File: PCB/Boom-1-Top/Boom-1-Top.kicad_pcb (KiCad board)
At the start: 4 copper layers, 345 x 165 mm, 768 parts, among them J1 DEBUG, J10 PIC_DEBUG, J11 PIC_DEBUG, J12 PIC_DEBUG, J13 PIC_DEBUG, J14 PIC_DEBUG, J15 USB_B_Micro, J16 SD_Card, J17 BT_DEBUG, J18 12V Supply, J19 3V3 Bypass, J2 MIDI IN, J20 5V Bypass, J3 MIDI OUT, J37 Osc1Conn, J38 Osc2Conn, J39 SubNoiseConn, J4 PIC_DEBUG, J40 FiltConn2, J41 EnvGenConn2, J42 EnvGenConn1, J43 FXConn1, J44 FiltConn1, J45 FXConn2, J46 EnvGenConn3, J5 PIC_DEBUG, J6 PIC_DEBUG, J7 PIC_DEBUG, J8 PIC_DEBUG, J9 PIC_DEBUG, Q1 AO3401A, Q2 AO3401A, SW1 Osc1SawEncoder, SW10 SubToOsc2FiltEncoder, SW11 Osc1ToOsc2FiltEncoder, SW12 Osc1FiltFreqEncoder, SW13 Osc2FiltFreqEncoder, SW14 SubFiltFreqEncoder, SW15 OscFiltEnvAttackEncoder, SW16 SubFiltEnvAttackEncoder, SW17 Osc1FiltResEncoder, SW18 Osc2FiltResEncoder, SW19 SubFiltResEncoder, SW2 Osc1SqrEncoder, SW20 OscFiltEnvDecayEncoder, SW21 SubFiltEnvDecayEncoder, SW22 OscFiltEnvSustainEncoder, SW23 SubFiltEnvSustainEncoder, SW24 Osc1DriveEncoder, SW25 Osc2DistortionEncoder, SW26 OscFiltEnvReleaseEncoder, SW27 SubFiltEnvReleaseEncoder, SW28 FXWetDryEncoder, SW29 SubAmpEnvAttackEncoder, SW3 Rotary_Encoder, SW30 OscAmpEnvAttackEncoder, SW31 FXControl1Encoder, SW32 SubAmpEnvDecayEncoder, SW33 OscAmpEnvDecayEncoder, SW34 FXControl2Encoder, SW35 SubAmpEnvSustainEncoder, SW36 OscAmpEnvSustainEncoder, SW37 FXControl3Encoder, SW38 FXFeedbackEncoder, SW39 SubAmpEnvReleaseEncoder, SW4 Rotary_Encoder_Switch, SW40 OscAmpEnvReleaseEncoder, SW41 Reset, SW43 Reset, SW5 Rotary_Encoder, SW53 Osc1TuneEncoder, SW6 SubToSubFiltEncoder, SW7 SubNoiseEncoder, U1 STM32F407VGTx, U10 DAC7678xPW, U11 PIC18F26Q43, U12 PIC18F26Q43, U13 PIC18F26Q43, U14 PIC18F26Q43, U15 PIC18F26Q43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

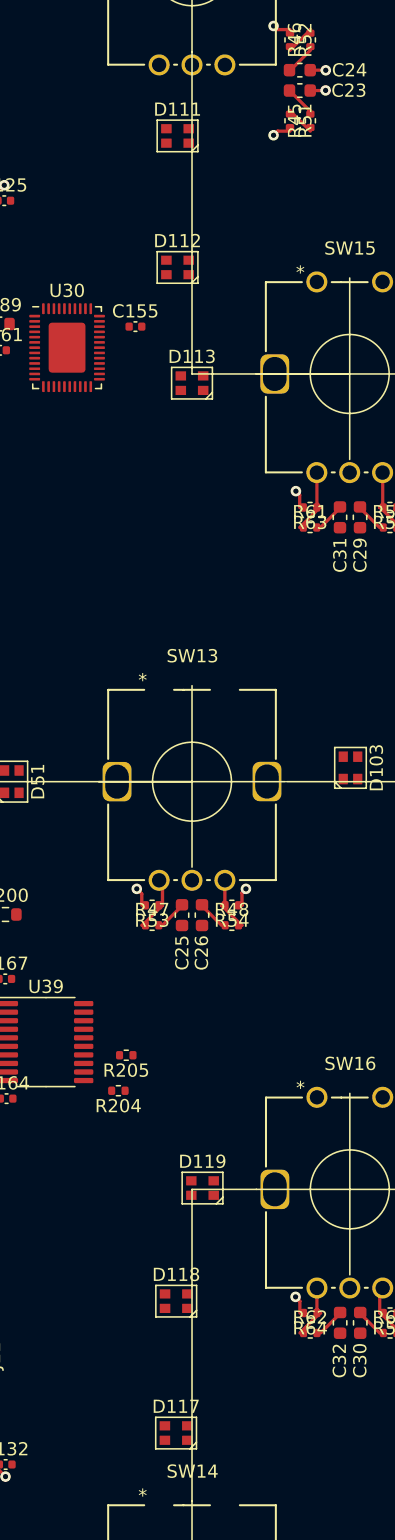
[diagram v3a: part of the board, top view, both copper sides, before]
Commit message: WIP, but crashed on open on discrete GPU machine
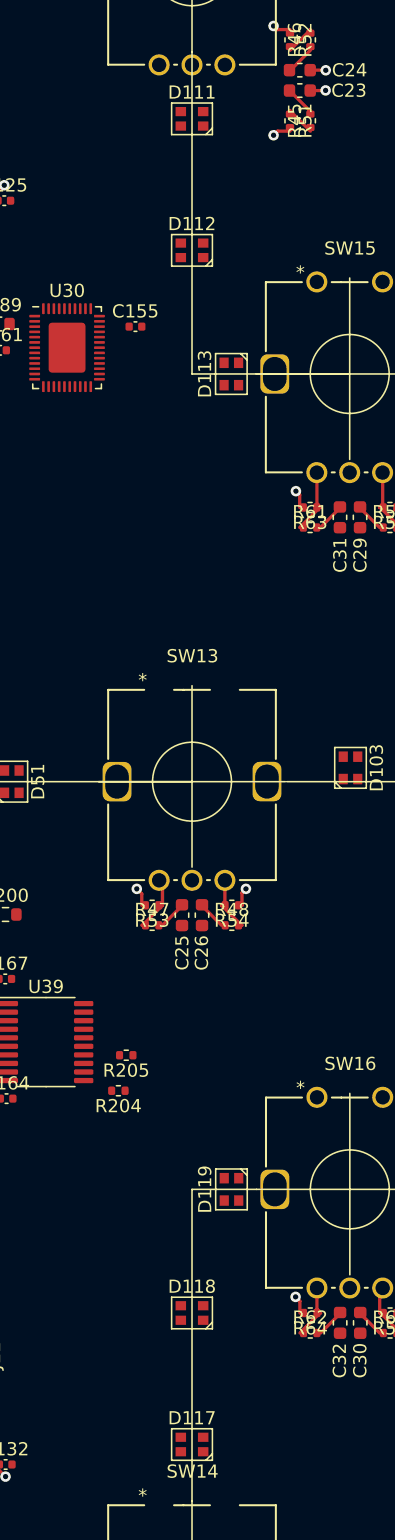
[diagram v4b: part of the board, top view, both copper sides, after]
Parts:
- moved D113 3.07 mm to (239.5, 156.2), turned to 90 degrees
- moved D119 2.20 mm to (239.5, 218.2), turned to 90 degrees
- moved D111 1.70 mm to (236.5, 136.8)
- moved D112 1.70 mm to (236.5, 146.8)
- moved D118 1.50 mm to (236.5, 227.6)
- moved D117 1.49 mm to (236.5, 237.6)
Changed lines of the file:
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@@
   )
   (module fm-b2020rgba-hg:FM-B2020RGBA-HG (layer F.Cu)
-    (at 237.3 218.1)
+    (at 239.5 218.2 90)
     (attr smd)
-    (fp_text reference D119 (at 0 -2) (layer F.SilkS)
+    (fp_text reference D119 (at 0 -2 90) (layer F.SilkS)
       (effects (font (size 1 1) (thickness 0.15)))
     )
-    (fp_text value SubFiltEnvLED3 (at 0 2.05) (layer F.Fab)
+    (fp_text value SubFiltEnvLED3 (at 0 2.05 90) (layer F.Fab)
       (effects (font (size 1 1) (thickness 0.15)))
     )
@@
     (fp_line (start 1.25 0.9) (end -1.25 0.9) (layer F.CrtYd) (width 0.12))
     (fp_line (start 1.25 0) (end 1.25 0.9) (layer F.CrtYd) (width 0.12))
-    (pad 4 smd rect (at 0.85 -0.55) (size 0.8 0.7) (layers F.Cu F.Paste F.Mask)
+    (pad 4 smd rect (at 0.85 -0.55 90) (size 0.8 0.7) (layers F.Cu F.Paste F.Mask)
       (net 859 L6G6))
-    (pad 3 smd rect (at -0.85 -0.55) (size 0.8 0.7) (layers F.Cu F.Paste F.Mask)
+    (pad 3 smd rect (at -0.85 -0.55 90) (size 0.8 0.7) (layers F.Cu F.Paste F.Mask)
       (net 1346 "Net-(D119-Pad3)"))
-    (pad 2 smd rect (at -0.85 0.55) (size 0.8 0.7) (layers F.Cu F.Paste F.Mask)
+    (pad 2 smd rect (at -0.85 0.55 90) (size 0.8 0.7) (layers F.Cu F.Paste F.Mask)
       (net 860 L6B6))
-    (pad 1 smd rect (at 0.85 0.55) (size 0.8 0.7) (layers F.Cu F.Paste F.Mask)
+    (pad 1 smd rect (at 0.85 0.55 90) (size 0.8 0.7) (layers F.Cu F.Paste F.Mask)
       (net 858 L6R6))
   )
   (module fm-b2020rgba-hg:FM-B2020RGBA-HG (layer F.Cu)
-    (at 235.3 226.7)
+    (at 236.5 227.6)
     (attr smd)
     (fp_text reference D118 (at 0 -2) (layer F.SilkS)
@@
   )
   (module fm-b2020rgba-hg:FM-B2020RGBA-HG (layer F.Cu)
-    (at 235.29 236.73)
+    (at 236.5 237.6)
     (attr smd)
     (fp_text reference D117 (at 0 -2) (layer F.SilkS)
@@
   )
   (module fm-b2020rgba-hg:FM-B2020RGBA-HG (layer F.Cu)
-    (at 236.5 156.9)
+    (at 239.49 156.2 90)
     (attr smd)
-    (fp_text reference D113 (at 0 -2) (layer F.SilkS)
+    (fp_text reference D113 (at 0 -2 90) (layer F.SilkS)
       (effects (font (size 1 1) (thickness 0.15)))
     )
-    (fp_text value OscFiltEnvLED3 (at 0 2.05) (layer F.Fab)
+    (fp_text value OscFiltEnvLED3 (at 0 2.05 90) (layer F.Fab)
       (effects (font (size 1 1) (thickness 0.15)))
     )
@@
     (fp_line (start 1.25 0.9) (end -1.25 0.9) (layer F.CrtYd) (width 0.12))
     (fp_line (start 1.25 0) (end 1.25 0.9) (layer F.CrtYd) (width 0.12))
-    (pad 4 smd rect (at 0.85 -0.55) (size 0.8 0.7) (layers F.Cu F.Paste F.Mask)
+    (pad 4 smd rect (at 0.85 -0.55 90) (size 0.8 0.7) (layers F.Cu F.Paste F.Mask)
       (net 850 L2G9))
-    (pad 3 smd rect (at -0.85 -0.55) (size 0.8 0.7) (layers F.Cu F.Paste F.Mask)
+    (pad 3 smd rect (at -0.85 -0.55 90) (size 0.8 0.7) (layers F.Cu F.Paste F.Mask)
       (net 1343 "Net-(D113-Pad3)"))
-    (pad 2 smd rect (at -0.85 0.55) (size 0.8 0.7) (layers F.Cu F.Paste F.Mask)
+    (pad 2 smd rect (at -0.85 0.55 90) (size 0.8 0.7) (layers F.Cu F.Paste F.Mask)
       (net 851 L2B9))
-    (pad 1 smd rect (at 0.85 0.55) (size 0.8 0.7) (layers F.Cu F.Paste F.Mask)
+    (pad 1 smd rect (at 0.85 0.55 90) (size 0.8 0.7) (layers F.Cu F.Paste F.Mask)
       (net 849 L2R9))
   )
   (module fm-b2020rgba-hg:FM-B2020RGBA-HG (layer F.Cu)
-    (at 235.4 148.1)
+    (at 236.5 146.8)
     (attr smd)
     (fp_text reference D112 (at 0 -2) (layer F.SilkS)
@@
   )
   (module fm-b2020rgba-hg:FM-B2020RGBA-HG (layer F.Cu)
-    (at 235.4 138.1)
+    (at 236.5 136.8)
     (attr smd)
     (fp_text reference D111 (at 0 -2) (layer F.SilkS)

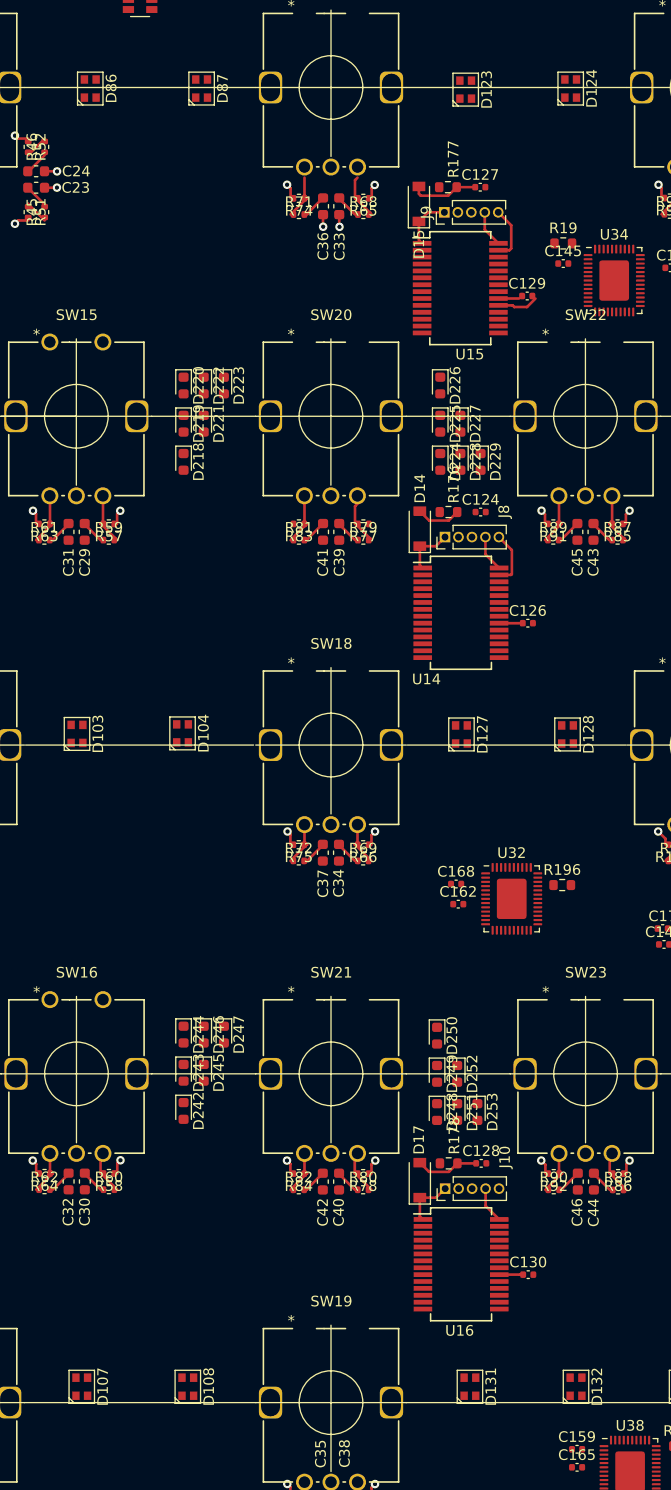
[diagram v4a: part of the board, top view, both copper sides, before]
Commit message: Aligned LEDs between osc1, osc2 and sub filter cut off and resonance knobs, and distortion/drive where appropriate
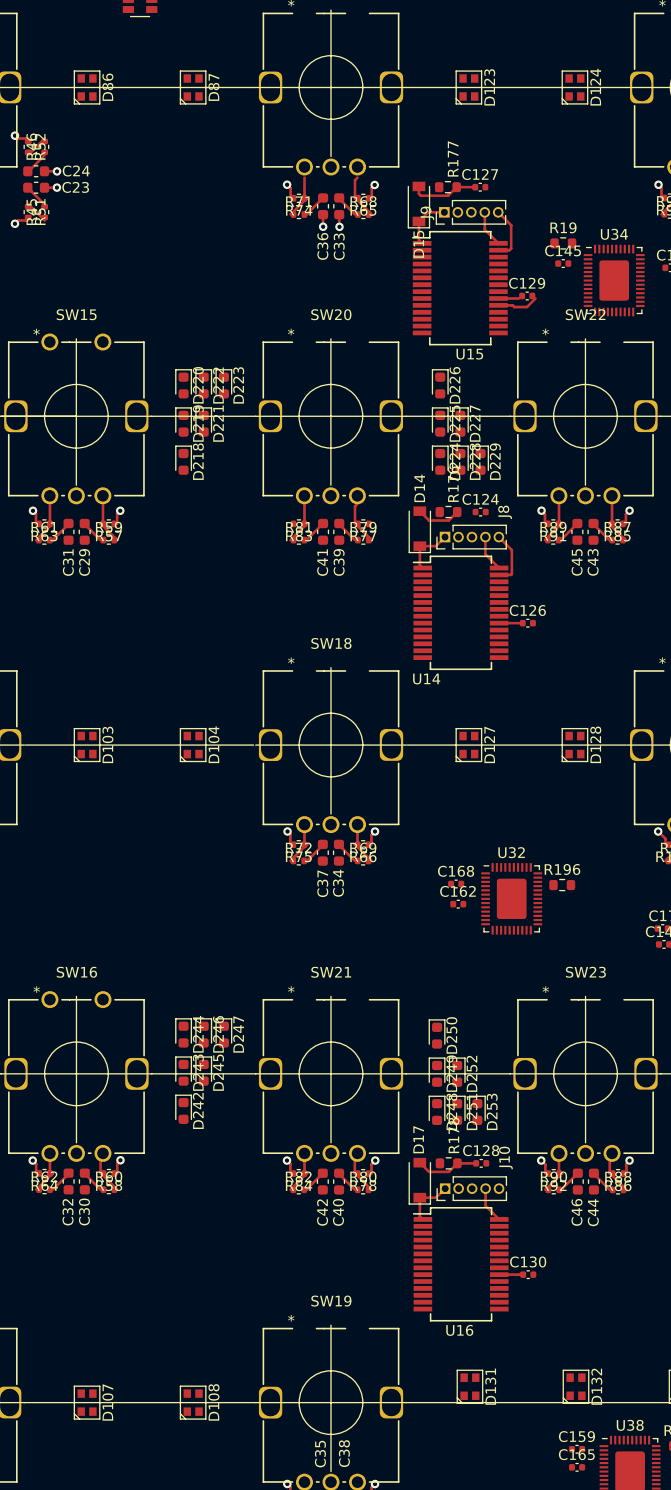
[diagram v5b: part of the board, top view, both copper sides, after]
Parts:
- moved D107 1.58 mm to (249.5, 249.2)
- moved D108 1.58 mm to (259.5, 249.2)
- moved D104 1.49 mm to (259.5, 187.2)
- moved D103 1.42 mm to (249.5, 187.2)
- moved D127 1.22 mm to (285.5, 187.2)
- moved D128 1.22 mm to (295.5, 187.2)
- moved D87 0.81 mm to (259.5, 125.2)
- moved D124 0.41 mm to (295.5, 125.2)
- moved D123 0.36 mm to (285.5, 125.2)
- moved D86 0.32 mm to (249.5, 125.2)

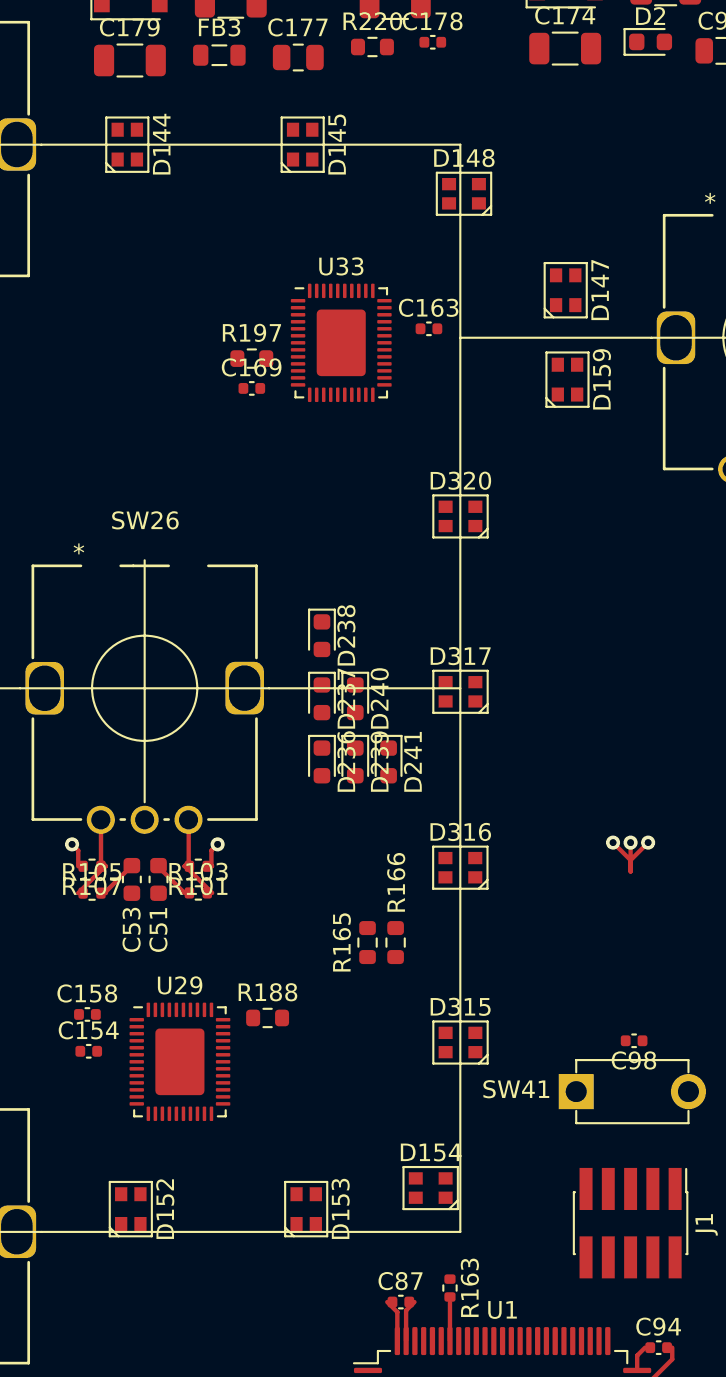
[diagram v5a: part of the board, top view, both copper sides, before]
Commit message: Aligned osc1 and osc2 filt to amp LEDs
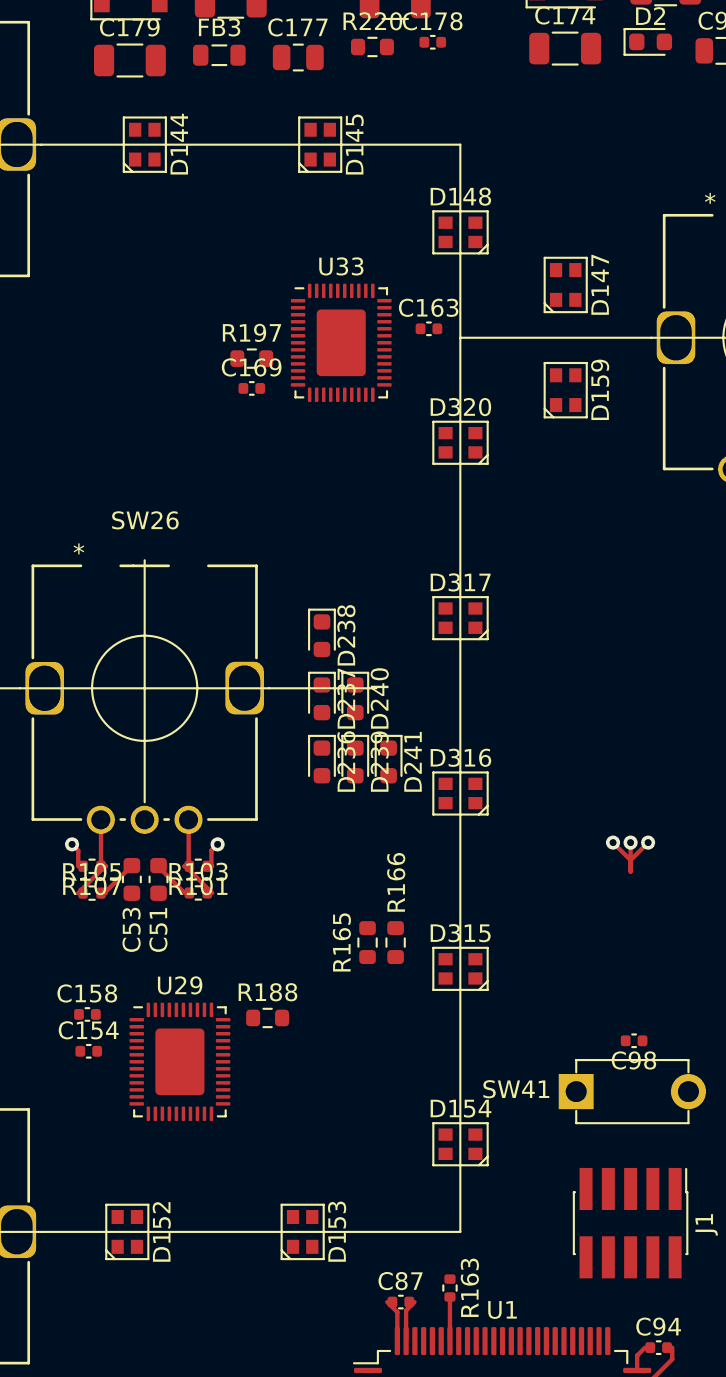
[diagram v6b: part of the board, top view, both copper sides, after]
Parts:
- moved D316 4.23 mm to (338.5, 162.2)
- moved D315 4.20 mm to (338.5, 172.2)
- moved D317 4.20 mm to (338.5, 152.2)
- moved D320 4.20 mm to (338.5, 142.2)
- moved D154 3.02 mm to (338.5, 182.2)
- moved D148 2.21 mm to (338.5, 130.2)
- moved D152 1.32 mm to (319.5, 187.2)
- moved D153 1.32 mm to (329.5, 187.2)
- moved D144 1.00 mm to (320.5, 125.2)
- moved D145 1.00 mm to (330.5, 125.2)
- moved D159 0.61 mm to (344.5, 139.2)
- moved D147 0.30 mm to (344.5, 133.2)
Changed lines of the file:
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@@
   )
   (module fm-b2020rgba-hg:FM-B2020RGBA-HG (layer F.Cu)
-    (at 338.5 146.4)
+    (at 338.5 142.2)
     (attr smd)
     (fp_text reference D320 (at 0 -2) (layer F.SilkS)
@@
   )
   (module fm-b2020rgba-hg:FM-B2020RGBA-HG (layer F.Cu)
-    (at 338.5 156.4)
+    (at 338.5 152.2)
     (attr smd)
     (fp_text reference D317 (at 0 -2) (layer F.SilkS)
@@
   )
   (module fm-b2020rgba-hg:FM-B2020RGBA-HG (layer F.Cu)
-    (at 338.49 166.43)
+    (at 338.5 162.2)
     (attr smd)
     (fp_text reference D316 (at 0 -2) (layer F.SilkS)
@@
   )
   (module fm-b2020rgba-hg:FM-B2020RGBA-HG (layer F.Cu)
-    (at 338.5 176.4)
+    (at 338.5 172.2)
     (attr smd)
     (fp_text reference D315 (at 0 -2) (layer F.SilkS)
@@
   )
   (module fm-b2020rgba-hg:FM-B2020RGBA-HG (layer F.Cu)
-    (at 344.6 138.6 270)
+    (at 344.5 139.2 270)
     (attr smd)
     (fp_text reference D159 (at 0 -2 90) (layer F.SilkS)
@@
   )
   (module fm-b2020rgba-hg:FM-B2020RGBA-HG (layer F.Cu)
-    (at 336.8 184.7)
+    (at 338.5 182.2)
     (attr smd)
     (fp_text reference D154 (at 0 -2) (layer F.SilkS)
@@
   )
   (module fm-b2020rgba-hg:FM-B2020RGBA-HG (layer F.Cu)
-    (at 329.7 185.9 270)
+    (at 329.5 187.2 270)
     (attr smd)
     (fp_text reference D153 (at 0 -2 90) (layer F.SilkS)
@@
   )
   (module fm-b2020rgba-hg:FM-B2020RGBA-HG (layer F.Cu)
-    (at 319.7 185.9 270)
+    (at 319.5 187.2 270)
     (attr smd)
     (fp_text reference D152 (at 0 -2 90) (layer F.SilkS)
@@
   )
   (module fm-b2020rgba-hg:FM-B2020RGBA-HG (layer F.Cu)
-    (at 338.7 128)
+    (at 338.5 130.2)
     (attr smd)
     (fp_text reference D148 (at 0 -2) (layer F.SilkS)
@@
       (effects (font (size 1 1) (thickness 0.15)))
     )
-    (fp_line (start 1.25 0) (end 1.25 0.9) (layer F.CrtYd) (width 0.12))
-    (fp_line (start 1.25 0.9) (end -1.25 0.9) (layer F.CrtYd) (width 0.12))
-    (fp_line (start -1.25 0.9) (end -1.25 -0.9) (layer F.CrtYd) (width 0.12))
-    (fp_line (start -1.25 -0.9) (end 1.25 -0.9) (layer F.CrtYd) (width 0.12))
-    (fp_line (start 1.25 -0.9) (end 1.25 0) (layer F.CrtYd) (width 0.12))
-    (fp_line (start -1.55 -1.2) (end -1.55 1.2) (layer F.SilkS) (width 0.12))
-    (fp_line (start -1.55 1.2) (end 1.55 1.2) (layer F.SilkS) (width 0.12))
-    (fp_line (start 1.55 1.2) (end 1.55 -1.2) (layer F.SilkS) (width 0.12))
-    (fp_line (start 1.55 -1.2) (end -1.55 -1.2) (layer F.SilkS) (width 0.12))
     (fp_line (start 1.05 1.2) (end 1.55 0.7) (layer F.SilkS) (width 0.12))
-    (pad 4 smd rect (at 0.85 -0.55) (size 0.8 0.7) (layers F.Cu F.Paste F.Mask)
-      (net 904 L3G3))
-    (pad 3 smd rect (at -0.85 -0.55) (size 0.8 0.7) (layers F.Cu F.Paste F.Mask)
-      (net 1361 "Net-(D148-Pad3)"))
-    (pad 2 smd rect (at -0.85 0.55) (size 0.8 0.7) (layers F.Cu F.Paste F.Mask)
-      (net 905 L3B3))
+    (fp_line (start 1.55 -1.2) (end -1.55 -1.2) (layer F.SilkS) (width 0.12))
+    (fp_line (start 1.55 1.2) (end 1.55 -1.2) (layer F.SilkS) (width 0.12))
+    (fp_line (start -1.55 1.2) (end 1.55 1.2) (layer F.SilkS) (width 0.12))
+    (fp_line (start -1.55 -1.2) (end -1.55 1.2) (layer F.SilkS) (width 0.12))
+    (fp_line (start 1.25 -0.9) (end 1.25 0) (layer F.CrtYd) (width 0.12))
+    (fp_line (start -1.25 -0.9) (end 1.25 -0.9) (layer F.CrtYd) (width 0.12))
+    (fp_line (start -1.25 0.9) (end -1.25 -0.9) (layer F.CrtYd) (width 0.12))
+    (fp_line (start 1.25 0.9) (end -1.25 0.9) (layer F.CrtYd) (width 0.12))
+    (fp_line (start 1.25 0) (end 1.25 0.9) (layer F.CrtYd) (width 0.12))
     (pad 1 smd rect (at 0.85 0.55) (size 0.8 0.7) (layers F.Cu F.Paste F.Mask)
       (net 903 L3R3))
+    (pad 2 smd rect (at -0.85 0.55) (size 0.8 0.7) (layers F.Cu F.Paste F.Mask)
+      (net 905 L3B3))
+    (pad 3 smd rect (at -0.85 -0.55) (size 0.8 0.7) (layers F.Cu F.Paste F.Mask)
+      (net 1361 "Net-(D148-Pad3)"))
+    (pad 4 smd rect (at 0.85 -0.55) (size 0.8 0.7) (layers F.Cu F.Paste F.Mask)
+      (net 904 L3G3))
   )
   (module fm-b2020rgba-hg:FM-B2020RGBA-HG (layer F.Cu)
-    (at 344.5 133.5 270)
+    (at 344.5 133.2 270)
     (attr smd)
     (fp_text reference D147 (at 0 -2 90) (layer F.SilkS)
@@
   )
   (module fm-b2020rgba-hg:FM-B2020RGBA-HG (layer F.Cu)
-    (at 329.5 125.2 270)
+    (at 330.5 125.2 270)
     (attr smd)
     (fp_text reference D145 (at 0 -2 90) (layer F.SilkS)
@@
   )
   (module fm-b2020rgba-hg:FM-B2020RGBA-HG (layer F.Cu)
-    (at 319.5 125.2 270)
+    (at 320.5 125.2 270)
     (attr smd)
     (fp_text reference D144 (at 0 -2 90) (layer F.SilkS)
@@
   )
   (gr_line (start 435.59 238.21) (end 445.75 238.21) (layer F.SilkS) (width 0.12))
-  (gr_line (start 327.59 156.2) (end 338.49 156.2) (layer F.SilkS) (width 0.12))
+  (gr_line (start 327.59 156.2) (end 333.7 156.2) (layer F.SilkS) (width 0.12))
   (gr_line (start 327.6 218.2) (end 336.6 218.2) (layer F.SilkS) (width 0.12))
   (gr_line (start 435.59 136.21) (end 444.73 136.21) (layer F.SilkS) (width 0.12))
